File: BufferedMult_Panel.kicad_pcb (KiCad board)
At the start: 2 copper layers, 20 x 128.5 mm, 10 parts, among them J2 IN_1, J3 OUT_1A, J4 OUT_1B, J5 OUT_1C, J6 IN_2, J7 OUT_2A, J8 OUT_2B, J9 OUT_2C

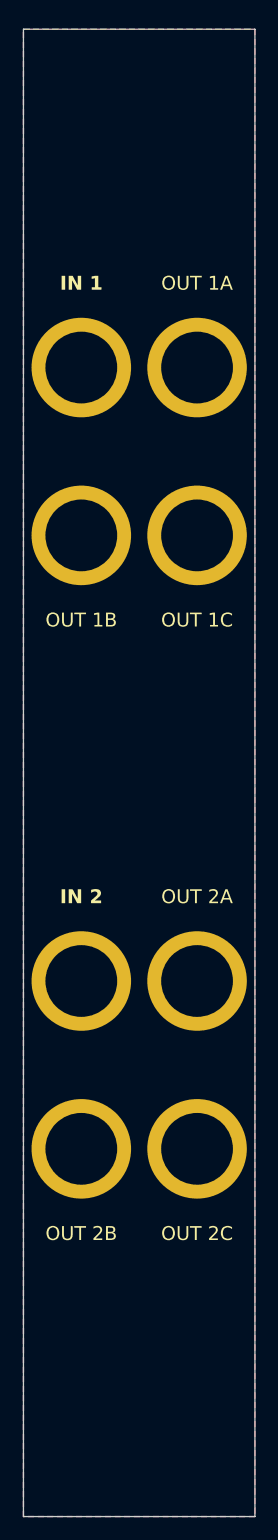
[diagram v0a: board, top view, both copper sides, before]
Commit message: Review 3-channel PCB layout and regenerate mated 4HP panel and production files
Following the expansion of BufferedMult.kicad_pcb to the full three-channel (1:3 / 1:6 / 1:9) 44-component layout, synchronize the front panel design, fabrication outputs, and design review documentation:

- Update generate_eurorack_panel.py to handle uniform 6-row (14.40 mm pitch) jack grids by placing front silkscreen labels at inter-row midpoints and positioning rear silkscreen text below the lowest jack row to prevent silkscreen overlap and solder-mask clipping.
- Regenerate BufferedMult_Panel.kicad_pcb and production/BufferedMult_Panel.zip (plus production/panel/ Gerbers and drills) with 12 grounded 6.2 mm jack cutouts aligned to the new 20.0 x 109.0 mm main PCB, and update FRONT_PANEL_GUIDE.md coordinates accordingly.
- Re-export production/BufferedMult.zip, netlist.ipc, bom.csv, positions.csv, and designators.csv so fabrication and SMT assembly files match the 44-component, 32-net 3-channel board.
- Update DESIGN_REVIEW.md with the 3-channel verification results (100% netlist/pad sync, 0 DRC and Gerber errors) and track adding the J1 -12V/red-stripe orientation callout and repository URL on silkscreen as required pre-fab items.
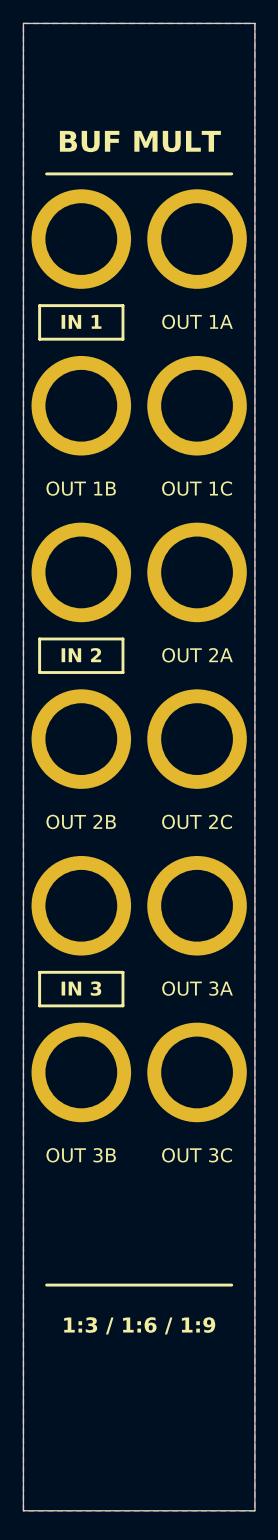
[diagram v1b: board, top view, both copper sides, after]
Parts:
- added J10: IN_3, Eurorack_Panel:JackHole_3.5mm_Thonkiconn_6.2mm, F.Cu at (25.0, 85.5)
- added J11: OUT_3A, Eurorack_Panel:JackHole_3.5mm_Thonkiconn_6.2mm, F.Cu at (35.0, 85.5)
- added J12: OUT_3B, Eurorack_Panel:JackHole_3.5mm_Thonkiconn_6.2mm, F.Cu at (25.0, 99.9)
- added J13: OUT_3C, Eurorack_Panel:JackHole_3.5mm_Thonkiconn_6.2mm, F.Cu at (35.0, 99.9)
- moved J8 35.4 mm to (25.0, 71.1)
- moved J9 35.4 mm to (35.0, 71.1)
- moved J6 35.3 mm to (25.0, 56.7)
- moved J7 35.3 mm to (35.0, 56.7)
- moved J4 11.2 mm to (25.0, 42.3)
- moved J5 11.2 mm to (35.0, 42.3)
- moved J2 11.1 mm to (25.0, 27.9)
- moved J3 11.1 mm to (35.0, 27.9)
- moved H1 0.50 mm to (27.5, 12.2)
- moved H2 0.50 mm to (27.5, 134.8)
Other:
- board text added: "1:3 / 1:6 / 1:9"
- board text added: "IN 3"
- board text added: "JLCJLCJLCJLC"
- board text added: "OUT 3A"
- board text added: "OUT 3B"
- board text added: "OUT 3C"

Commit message: Add labels and rebuild gerbers
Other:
- board text removed: "JLCJLCJLCJLC"
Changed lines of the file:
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@@
+	)
+	(gr_rect
+		(start 22 120)
+		(end 30 128)
+		(stroke
+			(width 0.1)
+			(type solid)
+		)
+		(fill yes)
+		(layer "B.SilkS")
 	)
 	(gr_rect
@@
 		(layer "B.SilkS")
 		(effects
-			(font
-				(size 1 1)
-				(thickness 0.15)
-			)
-			(justify mirror)
-		)
-	)
-	(gr_text "JLCJLCJLCJLC"
-		(at 30 115.75 0)
-		(layer "B.SilkS")
-		(effects

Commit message: Tidy up PCBs
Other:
- board text added: "TL074"
- board text removed: "1:3 / 1:6 / 1:9"
